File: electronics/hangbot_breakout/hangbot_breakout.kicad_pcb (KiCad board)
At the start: 2 copper layers, 52 x 44.5 mm, 14 parts, among them J1 CONN_02X10, J10 CONN_01X02, J11 CONN_01X02, J2 CONN_01X04, J3 CONN_01X02, J4 CONN_01X02, J5 CONN_01X02, J6 CONN_01X02, J7 CONN_01X02, J8 CONN_01X02, J9 CONN_01X02, P1 OSHW, P2 Hole, P3 Hole

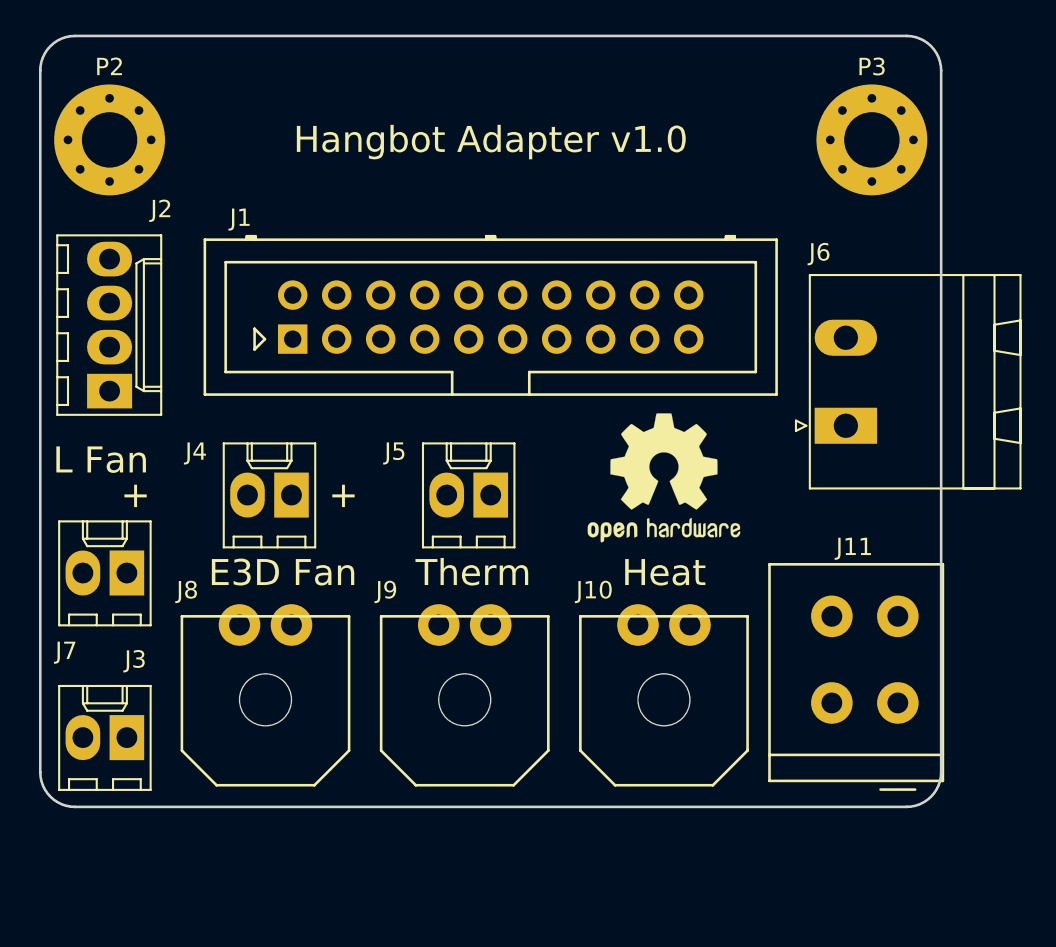
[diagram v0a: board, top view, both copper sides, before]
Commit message: Re-layout board to be NEMA-17 sized.
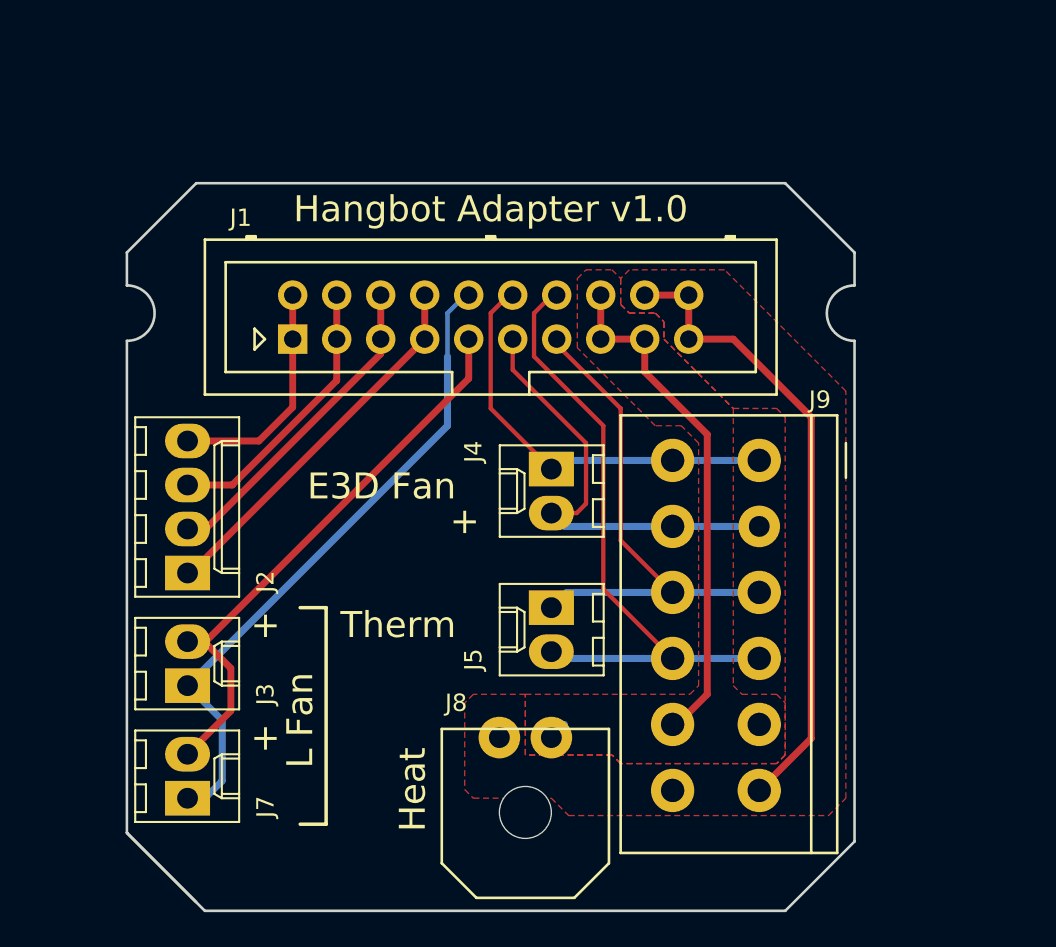
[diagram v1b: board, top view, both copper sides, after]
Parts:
- removed J11: CONN_01X02, TerminalBlocks_KF235:KF235_2Pin_3.81mm
- removed J6: CONN_01X02, Connectors_Phoenix:PhoenixContact_MSTBA-G_02x5.08mm_Angled
- removed the J8 at (139.5, 96.5)
- removed P2, P3: Hole, Mounting_Holes:MountingHole_3.2mm_M3_Pad_Via
- J9: value CONN_01X02 -> Conn_01x06; footprint Connectors_Molex_MicroFit:Molex_MicroFit_43650-0200_2Pin -> TerminalBlocks_TE:Spring_Horizontal_3.81mm_1-2834017-6
- P1: moved to B.Cu
- moved P1 20.1 mm to (142.5, 86.0), turned to 90 degrees
- moved J9 15.3 mm to (163.0, 87.0), turned to 90 degrees
- moved J4 15.1 mm to (156.0, 87.5), turned to 270 degrees
- moved J7 13.5 mm to (135.0, 106.5), turned to 90 degrees
- moved J2 11.4 mm to (135.0, 93.5)
- moved J8 10.3 mm to (154.5, 103.0)
- moved J5 7.38 mm to (156.0, 95.5), turned to 270 degrees
- moved J3 4.61 mm to (135.0, 100.0), turned to 90 degrees
- renumbered J10 to J8
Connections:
- J1 pad 1: MOT_A -> MOT_D
- J1 pad 2: MOT_A -> MOT_D
- J1 pad 3: MOT_B -> MOT_C
- J1 pad 4: MOT_B -> MOT_C
- J1 pad 5: MOT_C -> MOT_B
- J1 pad 6: MOT_C -> MOT_B
- J1 pad 7: MOT_D -> MOT_A
- J1 pad 8: MOT_D -> MOT_A
- J3 pad 1: LAYER_FAN_P -> LAYER_FAN_N
- J3 pad 2: LAYER_FAN_N -> LAYER_FAN_P
- J4 pad 1: HOT_ZONE_FAN_P -> HOT_ZONE_FAN_N
- J4 pad 2: HOT_ZONE_FAN_N -> HOT_ZONE_FAN_P
- J7 pad 1: LAYER_FAN_P -> LAYER_FAN_N
- J7 pad 2: LAYER_FAN_N -> LAYER_FAN_P
- J9 pad 1: THERMISTOR_A -> HOT_ZONE_FAN_N
- J9 pad 2: THERMISTOR_B -> HOT_ZONE_FAN_P
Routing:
- net LAYER_FAN_N: track 0.00 -> 38.1 mm
- net THERMISTOR_B: track 0.00 -> 37.1 mm
- net HEATER_B: track 0.00 -> 36.8 mm
- net LAYER_FAN_P: track 0.00 -> 33.9 mm
- net HEATER_A: track 0.00 -> 30.9 mm
- net THERMISTOR_A: track 0.00 -> 29.8 mm
- net HOT_ZONE_FAN_P: track 0.00 -> 25.8 mm
- net HOT_ZONE_FAN_N: track 0.00 -> 24.4 mm
- net MOT_A: track 0.00 -> 21.8 mm
- net MOT_B: track 0.00 -> 18.7 mm
- net MOT_C: track 0.00 -> 16.0 mm
- net MOT_D: track 0.00 -> 13.3 mm
- added copper zone on F.Cu, net HEATER_A
- added copper zone on F.Cu, net HEATER_B
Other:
- board size 52 x 44.5 mm -> 42 x 42 mm
- board text added: "github.com/google/ makerspace-partsbin electronics/ hangbot_breakout"
